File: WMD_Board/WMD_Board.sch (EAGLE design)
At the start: 32 parts, among them J1 EMPCB.SMAFSTJ.B.HT, U1 STM32L053C8T6, U2 BSS138, U3 RFM69HCW, U4 BSS138, Y2 ABS06-107-32.768KHZ-T

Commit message: Schematic work
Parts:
- added C2, C3, C4, C5: 0.1uF, SparkFun-Capacitors:0.1UF-0603-25V-(+80/-20%)
- added R10, R11, R12, R13, R14, R15, R7, R8: 10k, SparkFun-Resistors:10KOHM-0603-1/10W-1%
- added U$20: TS_DR_10, TST_Connnector:TS_DR_10
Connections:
- new net BTN1: C2.1, R8.1
- new net BTN2: C3.1, R11.1
- new net BTN3: C4.1, R13.1
- new net BTN4: C5.1, R15.1
- new net BTN_1_1: R7.1, R8.2, U$20.P$11
- new net BTN_1_2: C2.2
- new net BTN_2_1: R10.1, R11.2, U$20.P$12
- new net BTN_2_2: C3.2
- new net BTN_3_1: R12.1, R13.2, U$20.P$13
- new net BTN_3_2: C4.2
- new net BTN_4_1: R14.1, R15.2, U$20.P$14
- new net BTN_4_2: C5.2
- net 3.3V: now also R10.2, R12.2, R14.2, R7.2
- net GND: now also U$20.P$1, U$20.P$2, U$20.P$3, U$20.P$4
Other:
- note added: "PUSH BUTTONS"

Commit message: More Schematic Work
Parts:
- added C19, C20, C21: 0.1uF, SparkFun-Capacitors:0.1UF-0603-25V-(+80/-20%)
- added R16, R17: 4.7k, SparkFun-Resistors:1KOHM-0603-1/10W-1%
- added U5: M24512-DRMN8TP/K, M24512_EEPROM:M24512-DRMN8TP/K
- added U6: TPS72218DBVR, TPS72218DBVR_LDO:TPS72218DBVR
- U$20: value TS_DR_10 -> TS_DR_6; device TST_Connnector:TS_DR_10 -> TST_Connnector:TS_DR_6
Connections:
- net CS renamed LORA_CS
- net RST renamed LORA_RESET
- net SPI1_MISO renamed LORA_MISO
- net SPI1_MOSI renamed LORA_MOSI
- net SPI1_SCK renamed LORA_SCK
- removed net BTN_1_1: R7.1, R8.2, U$20.P$11
- removed net BTN_2_1: R10.1, R11.2, U$20.P$12
- removed net BTN_3_1: R12.1, R13.2, U$20.P$13
- removed net BTN_4_1: R14.1, R15.2, U$20.P$14
- removed net DIO5: U3.DIO5
- removed net GPS_RX: U1.PB11
- removed net GPS_TX: U1.PB10
- removed net MFIO: U$10.MFIO
- removed net N$2: R2.2, U1.PB12
- removed net RSTN: C14.1, U$10.RSTN
- new net BTN1_OUT: R7.1, R8.2, U$20.P$1
- new net BTN2_OUT: R10.1, R11.2, U$20.P$2
- new net BTN3_OUT: R12.1, R13.2, U$20.P$7
- new net BTN4_OUT: R14.1, R15.2, U$20.P$8
- new net HR_MFIO: U$10.MFIO, U1.PB4
- new net HR_RESET: C14.1, U$10.RSTN, U1.PB5
- new net LORA_DIO5: U1.PB1, U3.DIO5
- new net N$1: R2.2, U1.PB3
- new net OLED_CS: U$20.P$3, U1.PB12
- new net OLED_DC: U$20.P$5, U1.PB14
- new net OLED_MOSI: U$20.P$6, U1.PB15
- new net OLED_RESET: U$20.P$12, U1.PA8
- new net OLED_SCK: U$20.P$4, U1.PB13
- new net WC_EEPROM: U1.PB9, U5.WC
- net 1.8V: now also C20.1, U6.OUT
- net 3.3V: now also C19.1, C21.1, R16.1, R17.1, U$20.P$11, U5.VCC, U6.EN, U6.IN
- net BTN1: now also U1.PA0
- net BTN2: now also U1.PA1
- net BTN3: now also U1.PA2
- net BTN4: now also U1.PA3
- net DIO0: no longer U1.PB1
- net GND: now also C19.2, C20.2, C21.2, U$20.P$10, U$20.P$9, U5.E0, U5.E1, U5.E2, U5.VSS, U6.GND; no longer U$20.P$1, U$20.P$2, U$20.P$3, U$20.P$4
- net SCL_EEPROM: now also R17.2, U1.PB10, U5.SCL; no longer U1.PB13
- net SDA_EEPROM: now also R16.2, U1.PB11, U5.SDA; no longer U1.PB14
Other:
- note added: "TO HR SENSOR"
- moved on the sheet: C10, C15, C16, C7, C8, C9, LED1, R2

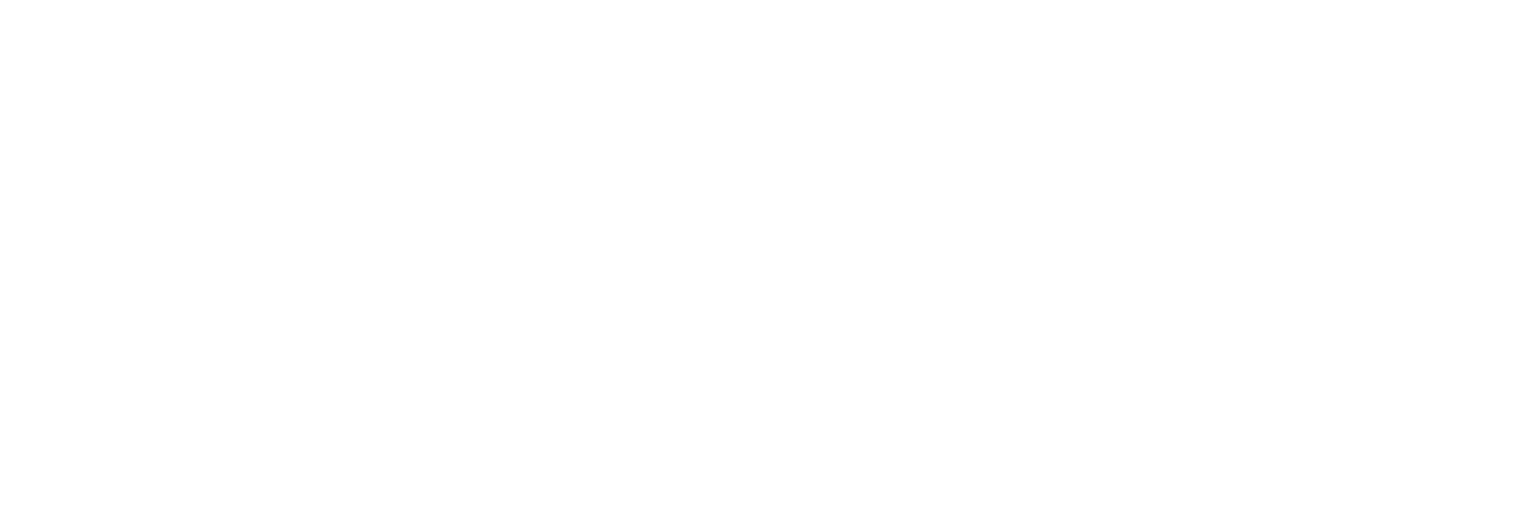
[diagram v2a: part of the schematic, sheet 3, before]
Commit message: added gps module
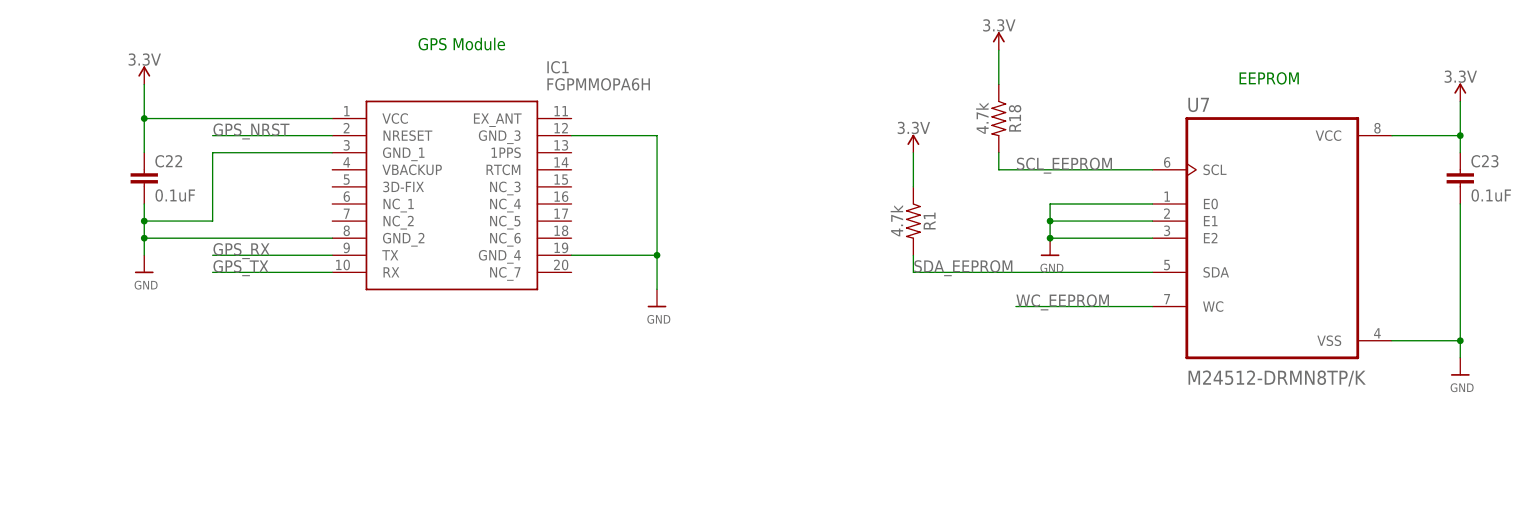
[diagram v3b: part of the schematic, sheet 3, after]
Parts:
- removed C19: 0.1uF, SparkFun-Capacitors:0.1UF-0603-25V-(+80/-20%)
- removed R16, R17: 4.7k, SparkFun-Resistors:1KOHM-0603-1/10W-1%
- removed U5: M24512-DRMN8TP/K, M24512_EEPROM:M24512-DRMN8TP/K
- added C22: 0.1uF, SparkFun-Capacitors:10UF-0603-6.3V-20%
- added C23: 0.1uF, SparkFun-Capacitors:0.1UF-0603-25V-(+80/-20%)
- added IC1: FGPMMOPA6H, FGPMMOPA6H:FGPMMOPA6H
- added R18: 4.7k, SparkFun-Resistors:1KOHM-0603-1/10W-1%
- added U7: M24512-DRMN8TP/K, M24512_EEPROM:M24512-DRMN8TP/K
- C17: value 4.7uF -> 0.1uF
- R1: value 1k -> 4.7k
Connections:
- new net GPS_NRST: IC1.NRESET, U1.PA11
- new net GPS_RX: IC1.TX, U1.PA10
- new net GPS_TX: IC1.RX, U1.PA9
- net 3.3V: now also C22.1, C23.1, IC1.VCC, R1.1, R18.1, U7.VCC; no longer C19.1, R1.2, R16.1, R17.1, U5.VCC
- net GND: now also C22.2, C23.2, IC1.GND_1, IC1.GND_2, IC1.GND_3, IC1.GND_4, U7.E0, U7.E1, U7.E2, U7.VSS; no longer C19.2, U5.E0, U5.E1, U5.E2, U5.VSS
- net NRST: no longer R1.1
- net SCL_EEPROM: now also R18.2, U7.SCL; no longer R17.2, U5.SCL
- net SDA_EEPROM: now also R1.2, U7.SDA; no longer R16.2, U5.SDA
- net WC_EEPROM: now also U7.WC; no longer U5.WC
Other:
- note added: "EEPROM"
- note added: "GPS Module"

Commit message: Added lots of schematic stuff
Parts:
- removed C2: 0.1uF, SparkFun-Capacitors:0.1UF-0603-25V-(+80/-20%)
- added C19, C24, C25: 10uF, SparkFun-Capacitors:1.0UF-0603-16V-10%
- added C26: 0.1uF, SparkFun-Capacitors:1.0UF-0603-16V-10%
- added L1: 2.2uH/NRH2412T2R2MNGH, microbuilder:INDUCTORNRH2412T
- added Q1: SI2323DS-T1-E3, SI2323DS-T1-E3:SI2323DS-T1-E3
- added R16: 100, SparkFun-Resistors:1KOHM-0603-1/10W-1%
- added U$22: TPS63001, TPS63001:TPS63001
- R7, R8: value 10k -> 100k; device SparkFun-Resistors:10KOHM-0603-1/10W-1% -> SparkFun-Resistors:1KOHM-0603-1/10W-1%
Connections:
- removed net BTN1: C2.1, R8.1, U1.PA0
- removed net BTN1_OUT: R7.1, R8.2, U$20.P$1
- removed net BTN_1_2: C2.2
- new net BTN_POWER_OUT: U$20.P$1
- new net N$2: L1.1, U$22.L1
- new net N$3: L1.2, U$22.L2
- new net N$4: R7.2, R8.1, U1.PA0
- new net N$7: C26.1, R16.1, U$22.EN, U$22.PS/SYNC, U$22.VINA
- new net VIN_BATTERY: Q1.D
- new net VIN_BB: C25.1, R16.2, U$22.VIN
- new net V_BAT_MEASURE: R7.1
- net 3.3V: now also C19.1, C24.1, U$22.FB, U$22.VOUT; no longer R7.2
- net GND: now also C19.2, C24.2, C25.2, C26.2, Q1.G, R8.2, U$22.GND, U$22.PGND, U$22.THERM, U1.BOOT0
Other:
- note added: "3.3V to 1.8V Linear Regulator"
- note added: "GND For Buttons"
- note added: "GND For OLED"
- note added: "Li-Ion to 3.3V Buck-Boost Converter"
- note added: "Reverse Voltage Protection"
- moved on the sheet: C20, C21, C3, R10, R11, R4, R5, R6, R7, R8, R9, U2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

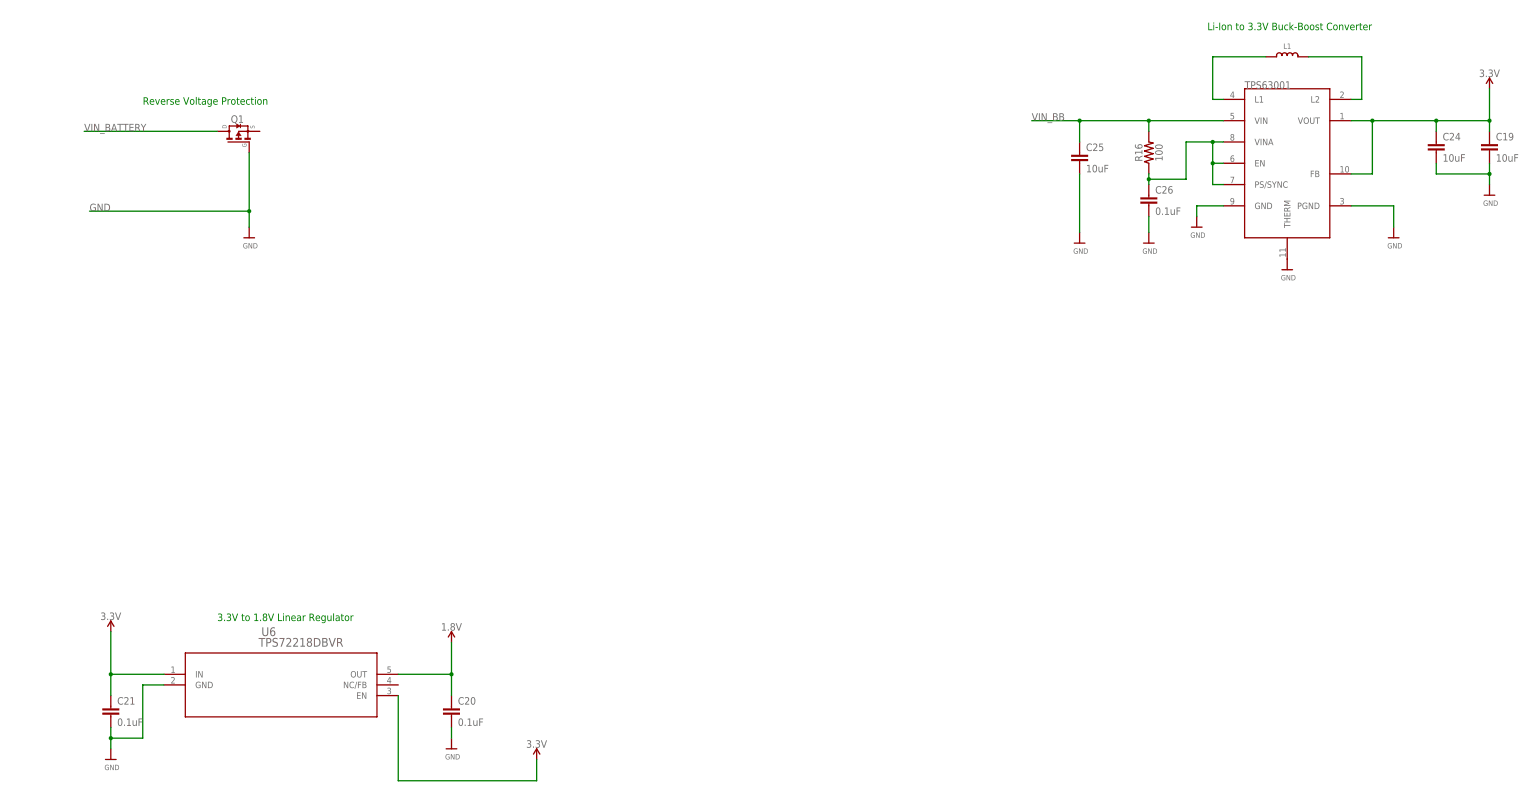
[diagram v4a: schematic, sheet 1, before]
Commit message: Board routing started
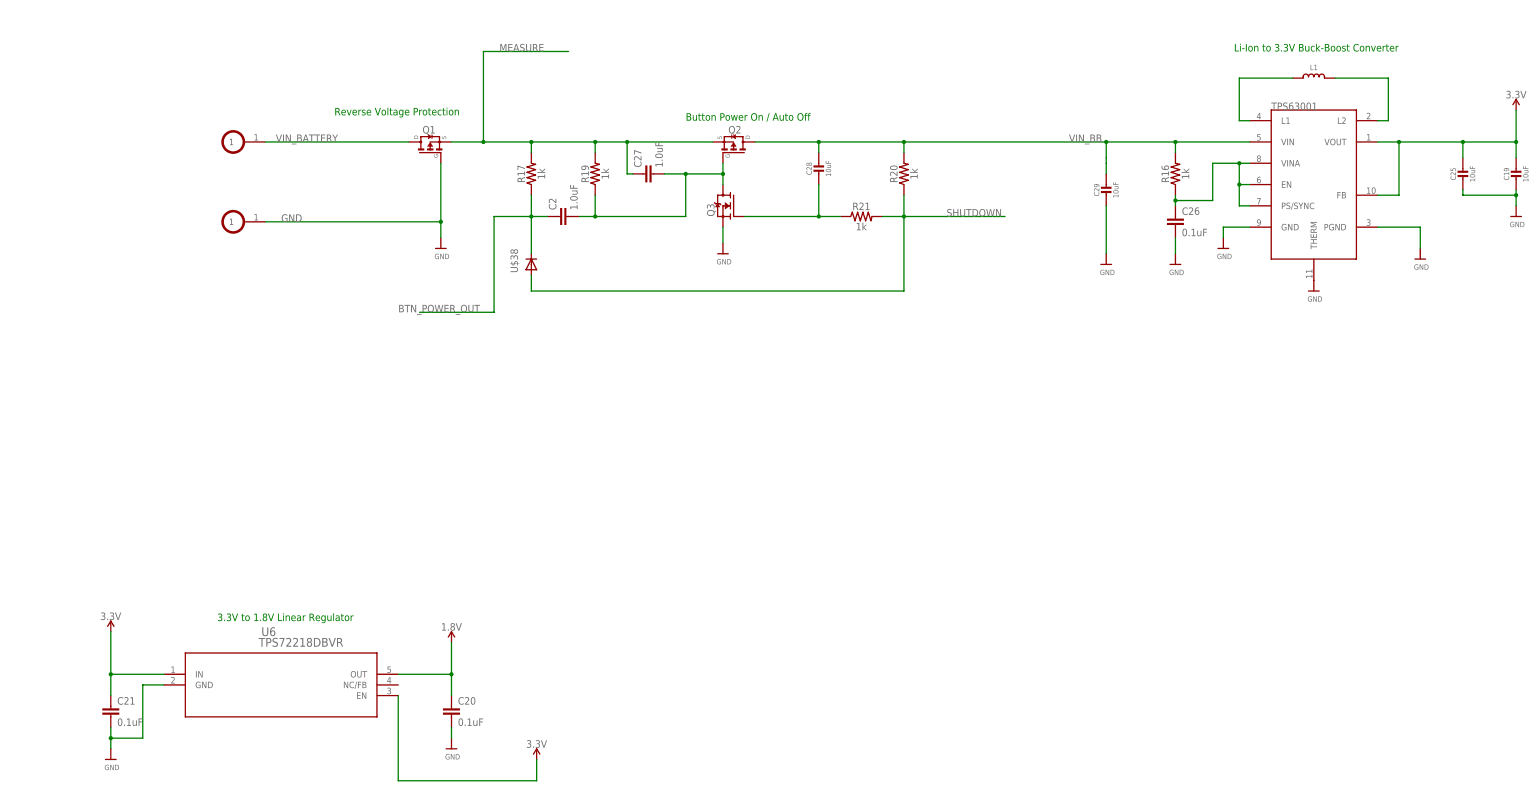
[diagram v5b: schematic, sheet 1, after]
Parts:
- removed C24: 10uF, SparkFun-Capacitors:1.0UF-0603-16V-10%
- removed JP1: (no value), microbuilder:HEADER-1X1ROUND
- added C2, C27: 1.0uF, SparkFun-Capacitors:1.0UF-0603-16V-10%
- added C28, C29: 10uF, microbuilder:CAP_CERAMIC0805-NOOUTLINE
- added Q2: SI2323DS-T1-E3, SI2323DS-T1-E3:SI2323DS-T1-E3
- added Q3: SI2312BDS, SI2312BDS:SI2312BDS
- added R17, R19, R20, R21: 1k, SparkFun-Resistors:1KOHM-0603-1/10W-1%
- added U$38: TS4148C_RZG, TS4148_RY:TS4148C_RZG
- added U$40, U$41: BATTERY_HOLE, Battery_Hole:BATTERY_HOLE
- C11, C13, C18: value 1uF -> 1.0uF
- C14: value 100nF -> 1.0uF
- C17: value 0.1uF -> 4.7uF
- C19, C25: device SparkFun-Capacitors:1.0UF-0603-16V-10% -> microbuilder:CAP_CERAMIC0805-NOOUTLINE
- C22: value 0.1uF -> 10uF
- R1, R18, R4, R5, R6, R9: value 4.7k -> 1k
- R16: value 100 -> 1k
- R3: value 10 -> 100k
- R7, R8: value 100k -> 1k
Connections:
- removed net V_BAT_MEASURE: R7.1
- new net MEASURE: C27.1, Q1.S, Q2.S, R17.2, R19.2, R7.1
- new net N$13: C28.2, Q3.G, R21.1
- new net N$14: C2.2, C27.2, Q2.G, Q3.D, R19.1
- new net SHUTDOWN: R20.1, R21.2, U$38.A, U1.PC13
- net 3.3V: now also C25.1; no longer C24.1
- net BTN_POWER_OUT: now also C2.1, R17.1, U$38.C
- net GND: now also C29.2, Q3.S, U$41.1; no longer C24.2
- net N$8: no longer JP1.1
- net VIN_BATTERY: now also U$40.1
- net VIN_BB: now also C28.1, C29.1, Q2.D, R20.2; no longer C25.1
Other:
- note added: "Button Power On / Auto Off"
- moved on the sheet: C11, C13, C14, C18, C19, C25, C26, L1, Q1, R16, R3, Y2

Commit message: lots of routing stuff
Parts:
- added C24: 0.01uF, SparkFun-Capacitors:1.0UF-0603-16V-10%
- added C30: 0.1uF, SparkFun-Capacitors:1.0UF-0603-16V-10%
- added J2: 5015680607, WMD_TO_HRF:5015680607
- R4, R5, R6, R9: value 1k -> 4.7k
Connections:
- removed net BTN_2_2: C3.2
- removed net BTN_3_2: C4.2
- removed net BTN_4_2: C5.2
- net 1.8V: now also J2.1
- net 3.3V: now also C24.1, C30.1, J2.3
- net GND: now also C24.2, C3.2, C30.2, C4.2, C5.2, J2.6
- net INT: now also J2.2
- net SCL_TO_HR_SENSOR: now also J2.5
- net SDA_TO_HR_SENSOR: now also J2.4
- net WC_EEPROM: now also U1.PB2; no longer U1.PB9
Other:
- note removed: "TO HR SENSOR"
- moved on the sheet: C19, C2, C25, C26, C27, C28, C29, L1, Q1, Q2, Q3, R16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

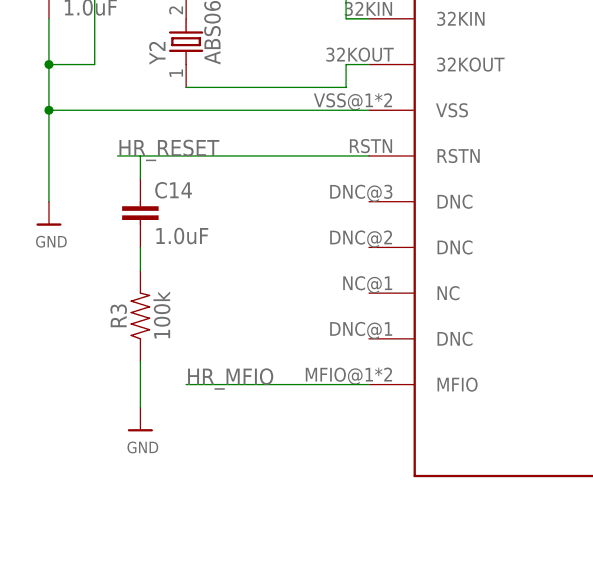
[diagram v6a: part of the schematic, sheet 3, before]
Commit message: noise snubber
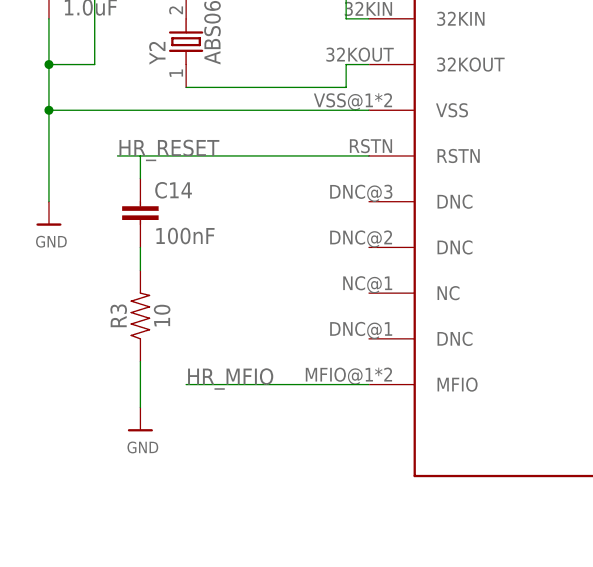
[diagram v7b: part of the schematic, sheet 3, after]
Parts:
- C14: value 1.0uF -> 100nF
- R3: value 100k -> 10
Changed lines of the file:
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@@
 <part name="U$17" library="microbuilder" deviceset="GND" device=""/>
 <part name="U$18" library="microbuilder" deviceset="GND" device=""/>
-<part name="C14" library="SparkFun-Capacitors" deviceset="1.0UF" device="-0603-16V-10%" value="1.0uF"/>
-<part name="R3" library="SparkFun-Resistors" deviceset="100KOHM" device="-0603-1/10W-1%" value="100k"/>
+<part name="C14" library="SparkFun-Capacitors" deviceset="1.0UF" device="-0603-16V-10%" value="100nF"/>
+<part name="R3" library="SparkFun-Resistors" deviceset="100KOHM" device="-0603-1/10W-1%" value="10"/>
 <part name="Y2" library="ABS06-107-32.768KHZ-T" deviceset="ABS06-107-32.768KHZ-T" device=""/>
 <part name="C18" library="SparkFun-Capacitors" deviceset="1.0UF" device="-0603-16V-10%" value="1.0uF"/>

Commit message: Routed
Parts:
- removed C5: 0.1uF, SparkFun-Capacitors:0.1UF-0603-25V-(+80/-20%)
- removed LED1: (no value), led:LEDCHIP-LED0805
- removed R14, R15: 10k, SparkFun-Resistors:10KOHM-0603-1/10W-1%
- removed R2: 1k, SparkFun-Resistors:1KOHM-0603-1/10W-1%
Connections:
- removed net BTN4: C5.1, R15.1, U1.PA3
- removed net BTN4_OUT: R14.1, R15.2, U$20.P$8
- removed net N$1: R2.2, U1.PB3
- removed net N$5: LED1.A, R2.1
- net 3.3V: no longer R14.2
- net BTN2: now also U1.PB8; no longer U1.PA1
- net BTN3: now also U1.PB9; no longer U1.PA2
- net GND: no longer C5.2, LED1.C
- net HR_MFIO: now also U1.PA15; no longer U1.PB4
- net SHUTDOWN: now also U1.PA2; no longer U1.PC13
